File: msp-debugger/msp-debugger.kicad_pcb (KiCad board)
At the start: 2 copper layers, 127 x 82.5 mm, 21 parts, among them J1 USB_B_Micro, J2 Conn_02x10, SW1 222ADVBA, SW2 222ADVBA, SW3 222ADVBA, SW4 222ADVBA, SW5 222ADVBA, SW6 222ADVBA, U1 ESP32-S2-SOLO, U2 NHD-0420H1Z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

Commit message: rough draft layout
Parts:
- moved SW3 104.9 mm to (190.5, 83.0), turned to 0 degrees
- moved SW1 92.1 mm to (105.4, 118.2)
- moved C3 58.5 mm to (125.8, 64.0)
- moved C6 36.9 mm to (88.8, 125.0)
- moved SW6 34.4 mm to (88.8, 118.2)
- moved J1 23.5 mm to (140.0, 61.0)
- moved C4 23.5 mm to (149.8, 60.0)
- moved D1 23.5 mm to (160.2, 64.0)
- moved F1 23.5 mm to (149.8, 66.0)
- moved U3 23.5 mm to (169.8, 64.2)
- moved SW2 13.4 mm to (117.2, 118.2)
- moved SW5 0.75 mm to (170.2, 118.2)
- moved C1 0.53 mm to (120.5, 61.2)
- moved C2 0.11 mm to (120.5, 66.8)
- turned SW4 to 0 degrees
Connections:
- SW1 pad 4: /RET SW -> /SET SW
- SW2 pad 4: /SET SW -> /RET SW
- SW4 pad 4: /DOWN DW -> /DOWN SW
- U1 pad 10: unconnected-(U1-GPIO17/U1TXD/ADC2_CH6/DAC_1-Pad10) -> /DB4
- U1 pad 11: unconnected-(U1-GPIO18/U1RXD/ADC2_CH7/DAC_2/CLK_OUT3-Pad11) -> /DB3
- U1 pad 12: unconnected-(U1-GPIO8/TOUCH8/ADC1_CH7-Pad12) -> /DB2
- U1 pad 15: /DB7 -> unconnected-(U1-GPIO3/TOUCH3/ADC1_CH2-Pad15)
- U1 pad 17: /DB6 -> /LCD RS
- U1 pad 18: /DB5 -> /LCD R/W
- U1 pad 19: /DB4 -> /DB0
- U1 pad 20: /DB3 -> /DB1
- U1 pad 21: /DB2 -> /TEST
- U1 pad 22: /LCD RS -> /RST
- U1 pad 23: /LCD R/W -> /TDO
- U1 pad 24: /DB0 -> /TDI
- U1 pad 25: /DB1 -> /TCK
- U1 pad 26: unconnected-(U1-GPIO45-Pad26) -> /TMS
- U1 pad 29: /DOWN DW -> /SET SW
- U1 pad 30: /UP SW -> unconnected-(U1-SPIDQS/GPIO37/FSPIQ-Pad30)
- U1 pad 31: /SET SW -> unconnected-(U1-GPIO38/FSPIWP-Pad31)
- U1 pad 4: /TMS -> unconnected-(U1-GPIO4/TOUCH4/ADC1_CH3-Pad4)
- U1 pad 5: /TCK -> /UP SW
- U1 pad 6: /TDI -> /DOWN SW
- U1 pad 7: /TDO -> /DB7
- U1 pad 8: /RST -> /DB6
- U1 pad 9: /TEST -> /DB5
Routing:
- net +3.3V: track 265.8 -> 332.2 mm, vias 0 -> 3
- net /TCK: track 126.5 -> 64.0 mm
- net /DOWN SW: track 0.00 -> 58.4 mm
- net /DB2: track 0.00 -> 53.7 mm
- net /DB3: track 0.00 -> 53.3 mm
- net /DB5: track 0.00 -> 52.4 mm
- net /DB4: track 0.58 -> 52.8 mm
- net unconnected-(U1-GPIO8/TOUCH8/ADC1_CH7-Pad12): track 52.1 -> 0.00 mm
- net /TMS: track 112.6 -> 60.8 mm
- net /TEST: track 112.7 -> 60.9 mm
- net /DB7: track 0.00 -> 51.4 mm
- net /DB6: track 0.58 -> 51.9 mm
- net unconnected-(U1-GPIO18/U1RXD/ADC2_CH7/DAC_2/CLK_OUT3-Pad11): track 50.8 -> 0.00 mm
- net /RST: track 107.2 -> 58.2 mm
- net unconnected-(U1-GPIO17/U1TXD/ADC2_CH6/DAC_1-Pad10): track 47.8 -> 0.00 mm
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- added copper zone on B.Cu, net GND
- added copper zone on F.Cu, net GND
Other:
- outline, holes or cut-outs redrawn

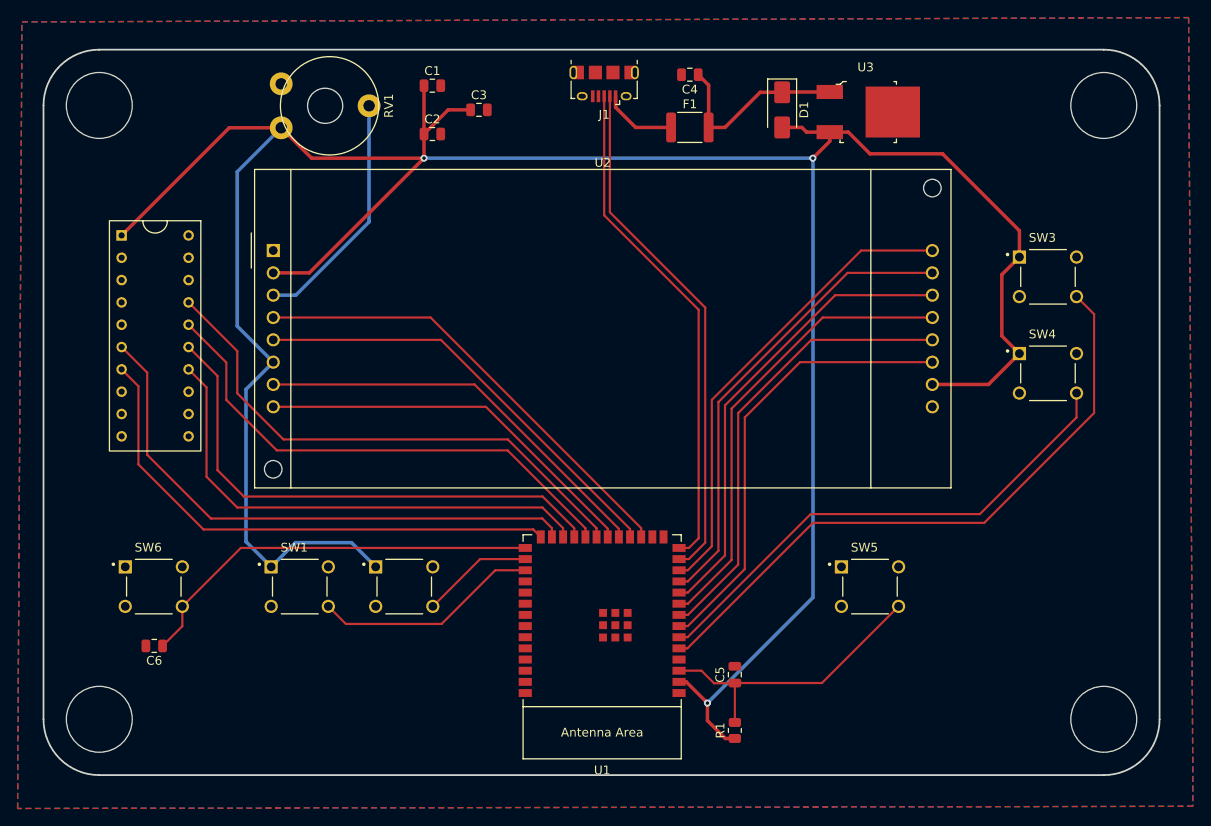
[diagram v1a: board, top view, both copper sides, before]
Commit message: add test points
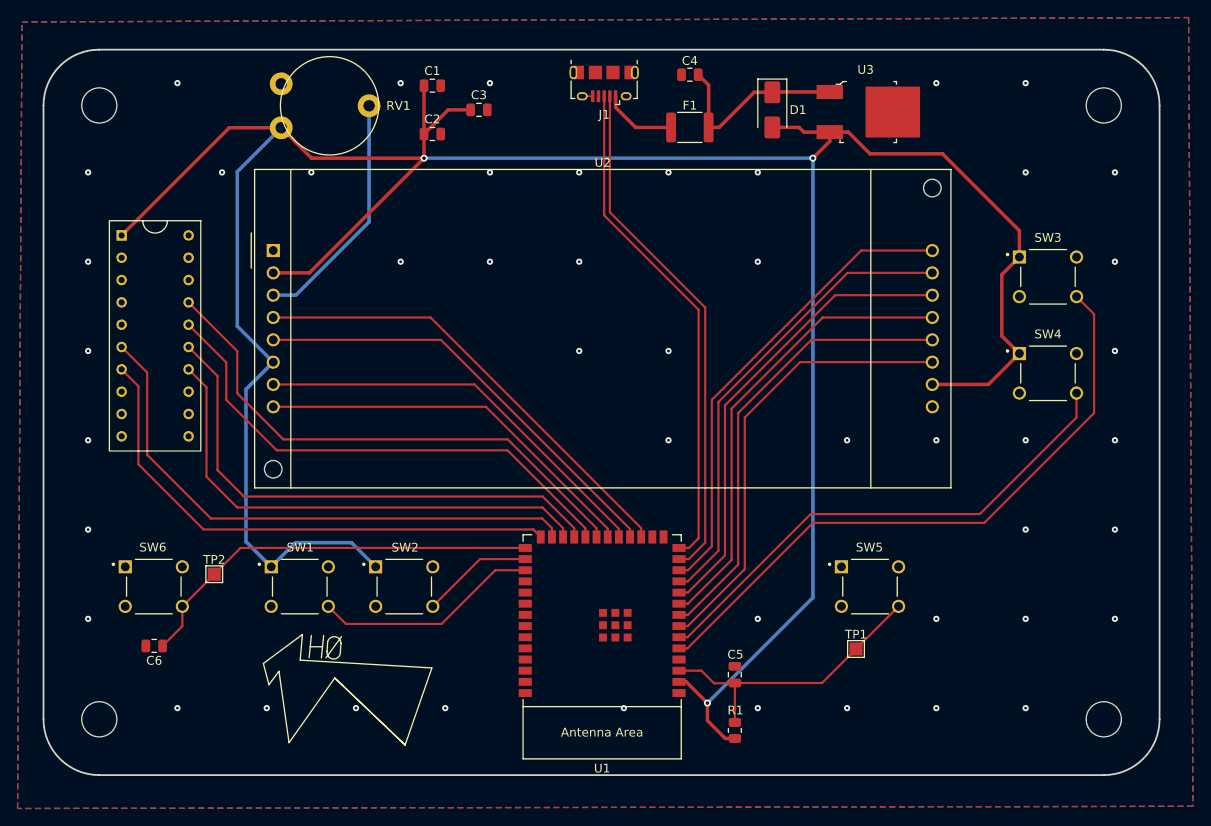
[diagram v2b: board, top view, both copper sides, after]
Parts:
- added TP1: TestPoint, TestPoint:TestPoint_Pad_1.5x1.5mm, F.Cu at (168.7, 125.3)
- added TP2: TestPoint, TestPoint:TestPoint_Pad_1.5x1.5mm, F.Cu at (95.6, 116.8)
- moved D1 1.12 mm to (159.1, 64.0)
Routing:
- net GND: track 0.00 -> 1.20 mm, vias 0 -> 47
- net +3.3V: track 332.2 -> 333.2 mm
- net /DB0: track 47.6 -> 47.1 mm
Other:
- outline, holes or cut-outs redrawn

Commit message: finalized pcb
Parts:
- renumbered SW4 to DOWN1, SW5 to ESP_ENABLE1, SW6 to ESP_PROGRAM1, SW2 to RETURN1, SW1 to SET1, SW3 to UP1
